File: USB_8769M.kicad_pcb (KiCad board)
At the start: 2 copper layers, 110 x 30 mm, 64 parts, among them J1 USB_B_Micro, J2 TagConnectTC2050, J3 Conn_02x07_Odd_Even, SW1 SW_Push, SW2 SW_Push, U1 LM27313XMF, U2 LP2985-3.3, U3 STM32F411RETx, U4 93LC66AT-IOT, U5 ULN2003ADR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

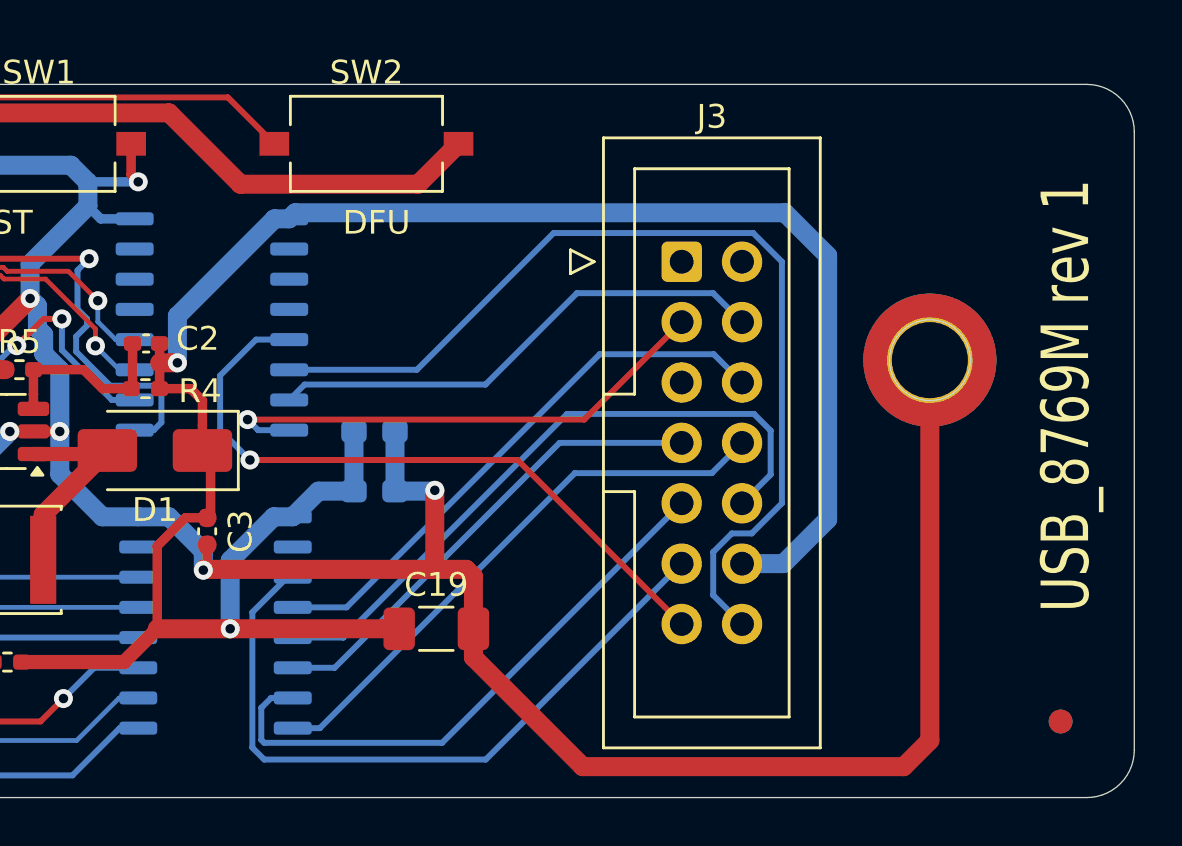
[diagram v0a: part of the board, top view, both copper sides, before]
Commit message: C3,5,7,17 had LCSC changed to rev 1.1
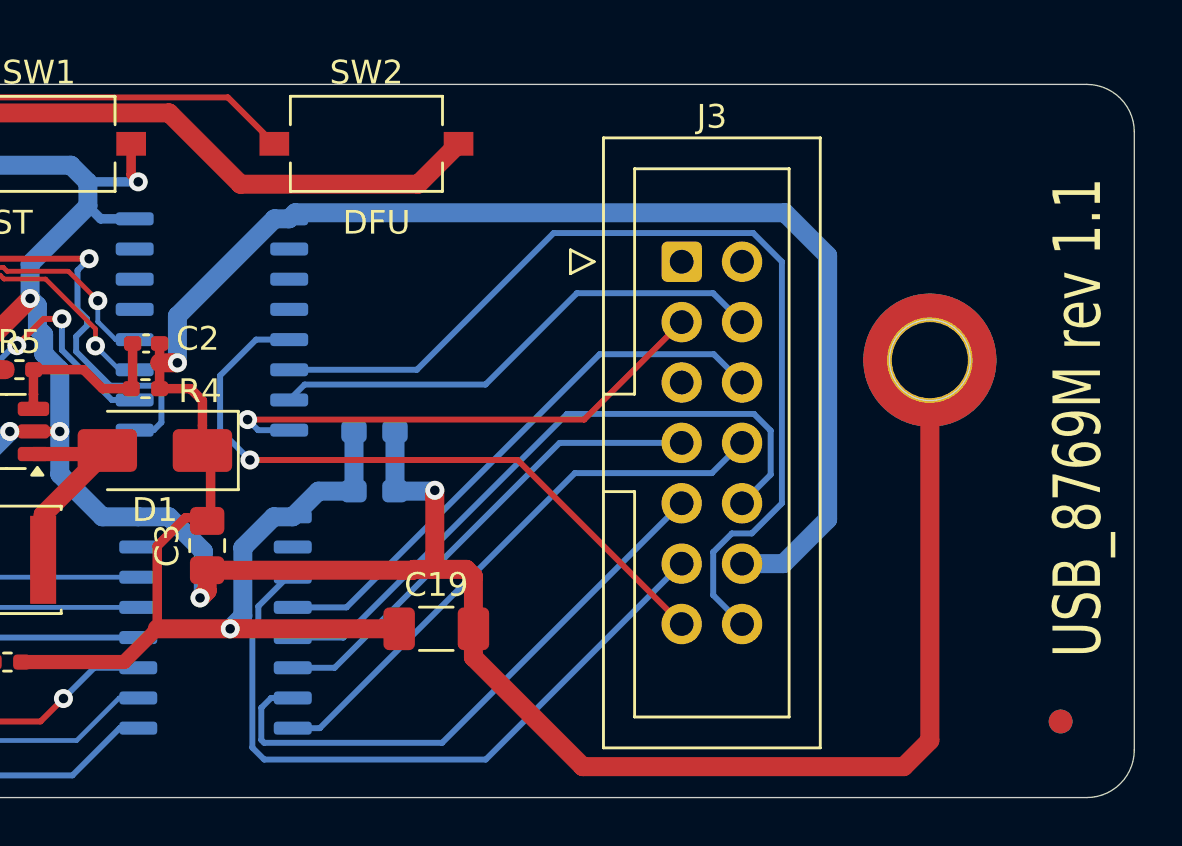
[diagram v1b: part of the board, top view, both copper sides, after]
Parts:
- C3: footprint Capacitor_SMD:C_0402_1005Metric_Pad0.74x0.62mm_HandSolder -> Capacitor_SMD:C_0805_2012Metric_Pad1.18x1.45mm_HandSolder
- moved C3 0.60 mm to (165.9, 104.0)
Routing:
- net GND: track 338.9 -> 340.1 mm
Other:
- board text added: "USB_8769M rev 1.1"
- board text removed: "USB_8769M rev 1"
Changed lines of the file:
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@@
 			)
 		)
-		(property "LCSC" "C1779"
+		(property "LCSC" "C106859"
 			(at 0 0 -90)
 			(unlocked yes)
@@
 			(net 1 "GND")
 			(pinfunction "GND")
-			(pintype "power_in")
+			(pintype "passive")
 		)
 		(pad "6" connect circle
@@
 		)
 	)
-	(footprint "Capacitor_SMD:C_0402_1005Metric_Pad0.74x0.62mm_HandSolder"
+	(footprint "Capacitor_SMD:C_0805_2012Metric_Pad1.18x1.45mm_HandSolder"
 		(layer "F.Cu")
-		(at 165.9 103.4 90)
-		(descr "Capacitor SMD 0402 (1005 Metric), square (rectangular) end terminal, IPC_7351 nominal with elongated pad for handsoldering. (Body size source: IPC-SM-782 page 76, https://www.pcb-3d.com/wordpress/wp-content/uploads/ipc-sm-782a_amendment_1_and_2.pdf), generated with kicad-footprint-generator")
+		(at 165.9 104 90)
+		(descr "Capacitor SMD 0805 (2012 Metric), square (rectangular) end terminal, IPC_7351 nominal with elongated pad for handsoldering. (Body size source: IPC-SM-782 page 76, https://www.pcb-3d.com/wordpress/wp-content/uploads/ipc-sm-782a_amendment_1_and_2.pdf, https://docs.google.com/spreadsheets/d/1BsfQQcO9C6DZCsRaXUlFlo91Tg2WpOkGARC1WS5S8t0/edit?usp=sharing), generated with kicad-footprint-generator")
 		(tags "capacitor handsolder")
 		(property "Reference" "C3"
-			(at 0 1.4 -90)
+			(at 0 -1.68 90)
 			(layer "F.SilkS")
 			(effects
@@
 		)
 		(property "Value" "4.7u"
-			(at 0 1.16 -90)
+			(at 0 1.68 90)
 			(layer "F.Fab")
 			(effects
@@
 			)
 		)
-		(property "Footprint" "Capacitor_SMD:C_0402_1005Metric_Pad0.74x0.62mm_HandSolder"
+		(property "Footprint" "Capacitor_SMD:C_0805_2012Metric_Pad1.18x1.45mm_HandSolder"
 			(at 0 0 90)
 			(unlocked yes)
@@
 		(attr smd)
 		(fp_line
-			(start -0.115835 -0.36)
-			(end 0.115835 -0.36)
+			(start -0.261252 -0.735)
+			(end 0.261252 -0.735)
 			(stroke
 				(width 0.12)
@@
 		)
 		(fp_line
-			(start -0.115835 0.36)
-			(end 0.115835 0.36)
+			(start -0.261252 0.735)
+			(end 0.261252 0.735)
 			(stroke
 				(width 0.12)
@@
 		)
 		(fp_line
-			(start 1.08 -0.46)
-			(end 1.08 0.46)
+			(start 1.88 -0.98)
+			(end 1.88 0.98)
 			(stroke
 				(width 0.05)
@@
 		)
 		(fp_line
-			(start -1.08 -0.46)
-			(end 1.08 -0.46)
+			(start -1.88 -0.98)
+			(end 1.88 -0.98)
 			(stroke
 				(width 0.05)
@@
 		)
 		(fp_line
-			(start 1.08 0.46)
-			(end -1.08 0.46)
+			(start 1.88 0.98)
+			(end -1.88 0.98)
 			(stroke
 				(width 0.05)
@@
 		)
 		(fp_line
-			(start -1.08 0.46)
-			(end -1.08 -0.46)
+			(start -1.88 0.98)
+			(end -1.88 -0.98)
 			(stroke
 				(width 0.05)
@@
 		)
 		(fp_line
-			(start 0.5 -0.25)
-			(end 0.5 0.25)
+			(start 1 -0.625)
+			(end 1 0.625)
 			(stroke
 				(width 0.1)
@@
 		)
 		(fp_line
-			(start -0.5 -0.25)
-			(end 0.5 -0.25)
+			(start -1 -0.625)
+			(end 1 -0.625)
 			(stroke
 				(width 0.1)
@@
 		)
 		(fp_line
-			(start 0.5 0.25)
-			(end -0.5 0.25)
+			(start 1 0.625)
+			(end -1 0.625)
 			(stroke
 				(width 0.1)
@@
 		)
 		(fp_line
-			(start -0.5 0.25)
-			(end -0.5 -0.25)
+			(start -1 0.625)
+			(end -1 -0.625)
 			(stroke
 				(width 0.1)
@@
 		)
 		(fp_text user "${REFERENCE}"
-			(at 0 0 -90)
+			(at 0 0 90)
 			(layer "F.Fab")
 			(effects
 				(font
-					(size 0.25 0.25)
-					(thickness 0.04)
+					(size 0.5 0.5)
+					(thickness 0.08)
 				)
 			)
 		)
 		(pad "1" smd roundrect
-			(at -0.5675 0 90)
-			(size 0.735 0.62)
+			(at -1.0375 0 90)
+			(size 1.175 1.45)
 			(layers "F.Cu" "F.Paste" "F.Mask")
-			(roundrect_rratio 0.25)
+			(roundrect_rratio 0.212766)
 			(net 1 "GND")
 			(pintype "passive")
 		)
 		(pad "2" smd roundrect
-			(at 0.5675 0 90)
-			(size 0.735 0.62)
+			(at 1.0375 0 90)
+			(size 1.175 1.45)
 			(layers "F.Cu" "F.Paste" "F.Mask")
-			(roundrect_rratio 0.25)
+			(roundrect_rratio 0.212766)
 			(net 3 "+VSW")
 			(pintype "passive")
 		)
-		(model "${KICAD8_3DMODEL_DIR}/Capacitor_SMD.3dshapes/C_0402_1005Metric.wrl"
+		(model "${KICAD8_3DMODEL_DIR}/Capacitor_SMD.3dshapes/C_0805_2012Metric.wrl"
 			(offset
 				(xyz 0 0 0)
@@
 			)
 		)
-		(property "LCSC" "C1779"
+		(property "LCSC" "C106859"
 			(at 0 0 180)
 			(unlocked yes)
@@
 			)
 		)
-		(property "LCSC" "C1779"
+		(property "LCSC" "C106859"
 			(at 0 0 0)
 			(unlocked yes)
@@
 		)
 	)
-	(gr_text "USB_8769M rev 1"
-		(at 203.2 106.8 90)
+	(gr_text "USB_8769M rev 1.1"
+		(at 203.7 108.7 90)
 		(layer "F.SilkS")
 		(effects
@@
 	)
 	(segment
+		(start 165.9 105.9)
+		(end 165.6 106.2)
+		(width 0.8)
+		(layer "F.Cu")
+		(net 1)
+	)
+	(segment
+		(start 174.5625 105.0375)
+		(end 165.9 105.0375)
+		(width 0.8)
+		(layer "F.Cu")
+		(net 1)
+	)
+	(segment
 		(start 147.4 85.725)
 		(end 145.7 85.725)
@@
 	)
 	(segment
-		(start 165.9 103.968)
-		(end 165.9 104.871033)
-		(width 0.4)
-		(layer "F.Cu")
-		(net 1)
-	)
-	(segment
 		(start 154.9 102.3)
 		(end 154.9 101.9)
@@
 	)
 	(segment
-		(start 174.6 105)
-		(end 165.771033 105)
-		(width 0.8)
-		(layer "F.Cu")
-		(net 1)
-	)
-	(segment
 		(start 121.85 99.5618)
 		(end 121.65 99.7618)
@@
 	)
 	(segment
-		(start 165.9 103.9675)
-		(end 165.9 103.968)
-		(width 0.8)
-		(layer "F.Cu")
-		(net 1)
-	)
-	(segment
 		(start 138.8 108.1)
 		(end 139.1 108.1)
@@
 	)
 	(segment
-		(start 165.9 104.871033)
-		(end 165.737999 105.033034)
-		(width 0.4)
-		(layer "F.Cu")
-		(net 1)
-	)
-	(segment
 		(start 132.432 110.468)
 		(end 132.4 110.435)
@@
 	)
 	(segment
-		(start 165.771033 105)
-		(end 165.737999 105.033034)
-		(width 0.8)
-		(layer "F.Cu")
-		(net 1)
-	)
-	(segment
 		(start 106.3 86.4)
 		(end 106.7 86)
@@
 	)
 	(segment
+		(start 174.6 105)
+		(end 174.5625 105.0375)
+		(width 0.8)
+		(layer "F.Cu")
+		(net 1)
+	)
+	(segment
 		(start 125.8 86.5)
 		(end 127 86.5)
@@
 	)
 	(segment
+		(start 165.9 105.0375)
+		(end 165.9 105.9)
+		(width 0.8)
+		(layer "F.Cu")
+		(net 1)
+	)
+	(segment
 		(start 116.3 98.8)
 		(end 117.7 98.8)
@@
 	)
 	(via
-		(at 165.737999 105.033034)
+		(at 165.6 106.2)
 		(size 0.8)
 		(drill 0.4)
@@
 	)
 	(segment
-		(start 165.737999 104.234999)
-		(end 165.737999 105.033034)
-		(width 0.8)
-		(layer "B.Cu")
-		(net 1)
-	)
-	(segment
 		(start 175.442026 101.71)
 		(end 175.476017 101.676009)
@@
 	)
 	(segment
+		(start 165.737999 106.062001)
+		(end 165.737999 104.234999)
+		(width 0.8)
+		(layer "B.Cu")
+		(net 1)
+	)
+	(segment
 		(start 127.97 106.3)
 		(end 128.07 106.4)
@@
 	)
 	(segment
+		(start 165.6 106.2)
+		(end 165.737999 106.062001)
+		(width 0.8)
+		(layer "B.Cu")
+		(net 1)
+	)
+	(segment
 		(start 129.429 102.575)
 		(end 129.104 102.9)
@@
 	)
 	(segment
-		(start 165.9 102.832)
-		(end 166.044 102.688)
-		(width 0.4)
-		(layer "F.Cu")
-		(net 3)
-	)
-	(segment
 		(start 165.7 98.95)
 		(end 165.7 100)
@@
 	)
 	(segment
-		(start 165.8995 102.832)
-		(end 165.9 102.8325)
-		(width 0.8)
-		(layer "F.Cu")
-		(net 3)
-	)
-	(segment
 		(start 166.868 107.5)
 		(end 166.867994 107.500006)
@@
 	)
 	(segment
-		(start 166.867994 104.622007)
+		(start 167.4 106.968)
 		(end 166.867994 107.500006)
 		(width 0.8)
@@
 	)
 	(segment
-		(start 169.5 102.79)
-		(end 168.700001 102.79)
+		(start 168.700001 102.79)
+		(end 167.4 104.090001)
 		(width 0.8)
 		(layer "B.Cu")
@@
 	)
 	(segment
+		(start 169.5 102.79)
+		(end 168.700001 102.79)
+		(width 0.8)
+		(layer "B.Cu")
+		(net 3)
+	)
+	(segment
 		(start 169.35 90.255)
 		(end 169.605 90)
@@
 	)
 	(segment
-		(start 190.2 90)
-		(end 192 91.8)
+		(start 167.4 104.090001)
+		(end 167.4 106.968)
 		(width 0.8)
 		(layer "B.Cu")
@@
 	)
 	(segment
-		(start 168.700001 102.79)
-		(end 166.867994 104.622007)
+		(start 190.2 90)
+		(end 192 91.8)
 		(width 0.8)
 		(layer "B.Cu")
@@
 	)
 	(segment
-		(start 167.8 106.806)
-		(end 169.276 105.33)
+		(start 167.8 107.490068)
+		(end 168.052 107.238068)
 		(width 0.25)
 		(layer "B.Cu")
@@
 	)
 	(segment
-		(start 177.62 113)
-		(end 168.3 113)
+		(start 167.8 112.5)
+		(end 167.8 107.490068)
 		(width 0.25)
 		(layer "B.Cu")
@@
 	)
 	(segment
-		(start 167.8 112.5)
-		(end 167.8 106.806)
+		(start 177.62 113)
+		(end 168.3 113)
 		(width 0.25)
 		(layer "B.Cu")
@@
 	)
 	(segment
-		(start 168.3 113)
-		(end 167.8 112.5)
+		(start 168.052 107.238068)
+		(end 168.052 106.554)
 		(width 0.25)
 		(layer "B.Cu")
@@
 		(width 0.25)
 		(layer "B.Cu")
+		(net 37)
+	)
+	(segment
+		(start 168.052 106.554)
+		(end 169.276 105.33)
+		(width 0.25)
+		(layer "B.Cu")
+		(net 37)
+	)
+	(segment
+		(start 168.3 113)
+		(end 167.8 112.5)
+		(width 0.25)
+		(layer "B.Cu")
